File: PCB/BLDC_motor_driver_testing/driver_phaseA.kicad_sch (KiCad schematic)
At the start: 22 parts, among them Q1 IRF540N, Q2 IRF540N, U2 IR2104, U3 INA240A2D, U4 LMV393

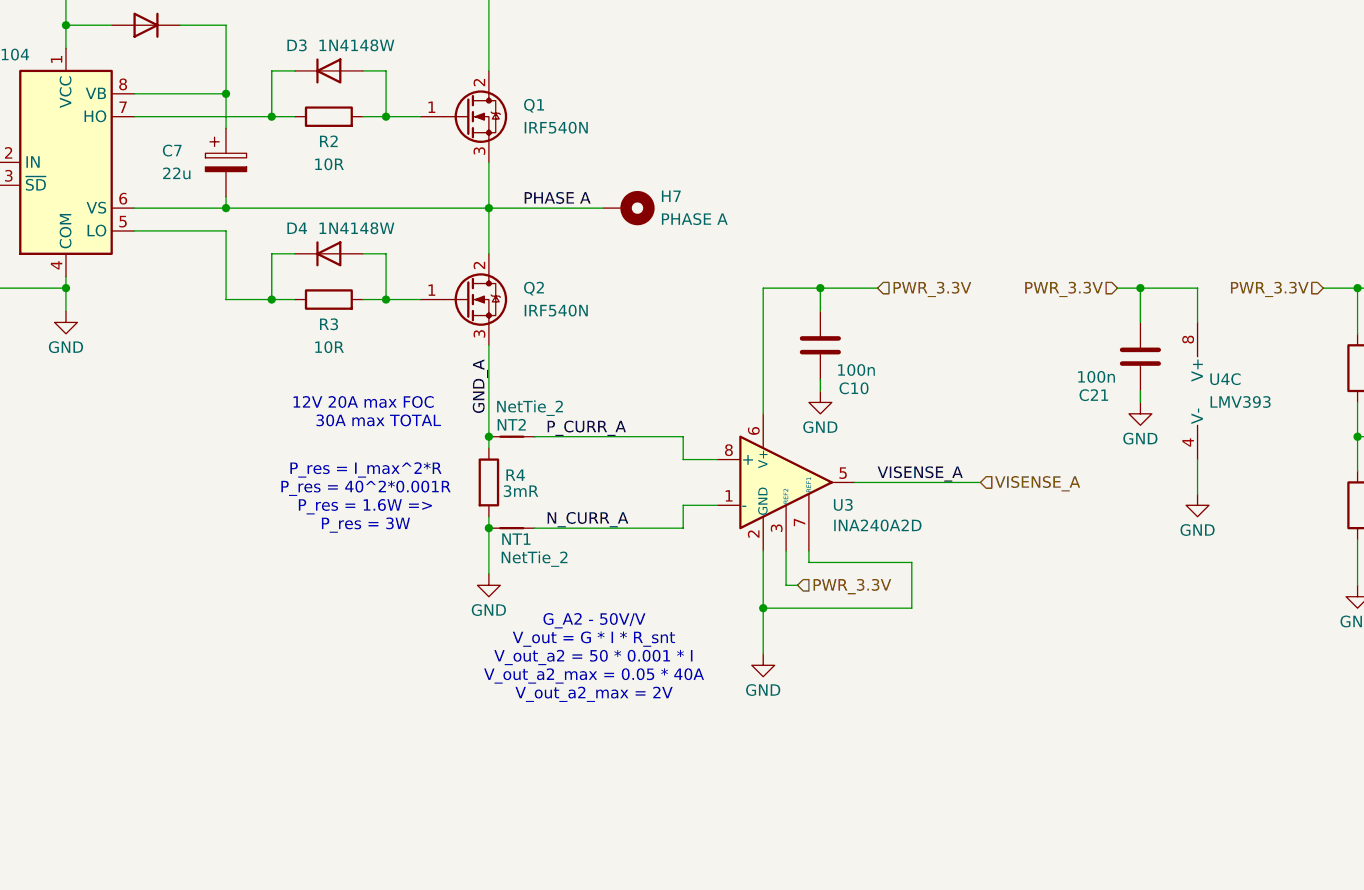
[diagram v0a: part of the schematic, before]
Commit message: selected bootstrap caps and shunt resistor and csa gain
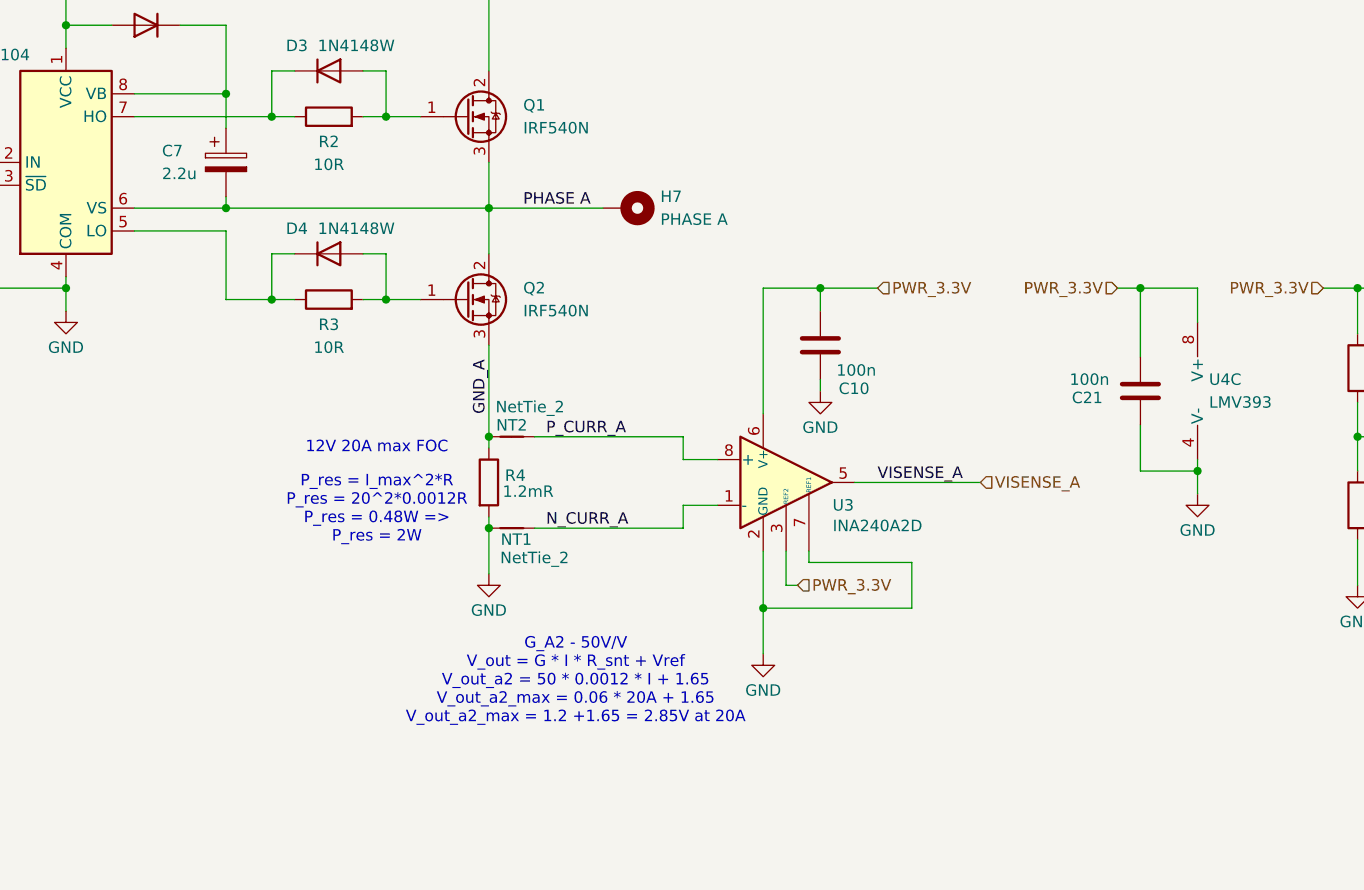
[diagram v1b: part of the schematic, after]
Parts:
- C7: value 22u -> 2.2u; footprint Capacitor_Tantalum_SMD:CP_EIA-3216-18_Kemet-A_HandSolder -> Capacitor_SMD:C_0805_2012Metric_Pad1.18x1.45mm_HandSolder
- R4: value 3mR -> 1.2mR
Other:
- note added: "12V 20A max FOC"
- note added: "G_A2 - 50V/V V_out = G * I * R_snt + Vref V_out_a2 = 50 * 0.0012 * I + 1.65 V_out_a2_max = 0.06 * 20A + 1.65 V_out_a2_max = 1.2 +1.65 = 2.85V at 20A"
- note added: "P_res = I_max^2*R P_res = 20^2*0.0012R P_res = 0.48W => P_res = 2W"
- note removed: "12V 20A max FOC 30A max TOTAL"
- note removed: "G_A2 - 50V/V V_out = G * I * R_snt V_out_a2 = 50 * 0.001 * I V_out_a2_max = 0.05 * 40A V_out_a2_max = 2V"
- note removed: "P_res = I_max^2*R P_res = 40^2*0.001R P_res = 1.6W => P_res = 3W"
- moved on the sheet: C21
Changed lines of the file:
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@@
 	(generator_version "9.0")
 	(paper "A4")
-	(text "12V 20A max FOC\n	  30A max TOTAL"
+	(text "12V 20A max FOC"
 		(exclude_from_sim no)
-		(at 99.06 107.95 0)
+		(at 100.584 111.76 0)
 		(effects
 			(font
@@
 		)
 	)
-	(text "G_A2 - 50V/V\nV_out = G * I * R_snt\nV_out_a2 = 50 * 0.001 * I\nV_out_a2_max = 0.05 * 40A\nV_out_a2_max = 2V"
+	(text "G_A2 - 50V/V\nV_out = G * I * R_snt + Vref\nV_out_a2 = 50 * 0.0012 * I + 1.65\nV_out_a2_max = 0.06 * 20A + 1.65\nV_out_a2_max = 1.2 +1.65 = 2.85V at 20A"
 		(exclude_from_sim no)
-		(at 124.714 135.128 0)
+		(at 122.682 137.668 0)
 		(effects
 			(font
@@
 		)
 	)
-	(text "P_res = I_max^2*R\nP_res = 40^2*0.001R\nP_res = 1.6W =>\nP_res = 3W"
+	(text "BLDC Driver Phase B"
 		(exclude_from_sim no)
-		(at 99.314 117.348 0)
+		(at 197.358 189.738 0)
 		(effects
 			(font
@@
 		)
 	)
-	(text "BLDC Driver Phase B"
+	(text "P_res = I_max^2*R\nP_res = 20^2*0.0012R\nP_res = 0.48W =>\nP_res = 2W"
 		(exclude_from_sim no)
-		(at 197.358 189.738 0)
+		(at 100.584 118.618 0)
 		(effects
 			(font
@@
 	)
 	(junction
+		(at 191.77 114.3)
+		(diameter 0)
+		(color 0 0 0 0)
+	)
+	(junction
 		(at 143.51 129.54)
 		(diameter 0)
@@
 	(wire
 		(pts
-			(xy 191.77 116.84) (xy 191.77 113.03)
+			(xy 191.77 116.84) (xy 191.77 114.3)
 		)
 		(stroke
@@
 	(wire
 		(pts
+			(xy 185.42 109.22) (xy 185.42 114.3)
+		)
+		(stroke
+			(width 0)
+			(type default)
+		)
+	)
+	(wire
+		(pts
 			(xy 143.51 129.54) (xy 160.02 129.54)
 		)
@@
 	(wire
 		(pts
-			(xy 185.42 105.41) (xy 185.42 106.68)
-		)
-		(stroke
-			(width 0)
-			(type default)
-		)
-	)
-	(wire
-		(pts
 			(xy 118.11 120.65) (xy 134.62 120.65)
 		)
@@
 	(wire
 		(pts
+			(xy 191.77 114.3) (xy 191.77 113.03)
+		)
+		(stroke
+			(width 0)
+			(type default)
+		)
+	)
+	(wire
+		(pts
 			(xy 91.44 69.85) (xy 88.9 69.85)
 		)
@@
 	(wire
 		(pts
-			(xy 185.42 97.79) (xy 185.42 93.98)
+			(xy 185.42 101.6) (xy 185.42 93.98)
 		)
 		(stroke
@@
 	(wire
 		(pts
+			(xy 185.42 114.3) (xy 191.77 114.3)
+		)
+		(stroke
+			(width 0)
+			(type default)
+		)
+	)
+	(wire
+		(pts
 			(xy 148.59 124.46) (xy 160.02 124.46)
 		)
@@
 			)
 		)
-		(property "Value" "3mR"
+		(property "Value" "1.2mR"
 			(at 114.554 116.586 0)
 			(effects
@@
 			)
 		)
-		(property "Value" "22u"
+		(property "Value" "2.2u"
 			(at 76.708 81.28 0)
 			(effects
@@
 			)
 		)
-		(property "Footprint" "Capacitor_Tantalum_SMD:CP_EIA-3216-18_Kemet-A_HandSolder"
+		(property "Footprint" "Capacitor_SMD:C_0805_2012Metric_Pad1.18x1.45mm_HandSolder"
 			(at 84.7852 83.82 0)
 			(effects
@@
 	(symbol
 		(lib_id "Device:C")
-		(at 185.42 101.6 0)
+		(at 185.42 105.41 0)
 		(unit 1)
 		(exclude_from_sim no)
@@
 		(dnp no)
 		(property "Reference" "C21"
-			(at 178.562 105.918 0)
+			(at 177.8 106.172 0)
 			(effects
 				(font
@@
 		)
 		(property "Value" "100n"
-			(at 178.308 103.886 0)
+			(at 177.546 104.14 0)
 			(effects
 				(font
@@
 		)
 		(property "Footprint" "Capacitor_SMD:C_0805_2012Metric_Pad1.18x1.45mm_HandSolder"
-			(at 186.3852 105.41 0)
+			(at 186.3852 109.22 0)
 			(effects
 				(font
@@
 		)
 		(property "Datasheet" "~"
-			(at 185.42 101.6 0)
+			(at 185.42 105.41 0)
 			(effects
 				(font
@@
 		)
 		(property "Description" "Unpolarized capacitor"
-			(at 185.42 101.6 0)
+			(at 185.42 105.41 0)
 			(effects
 				(font
@@
 					(unit 1)
 				)
-			)
-		)
-	)
-	(symbol
-		(lib_id "power:GND")
-		(at 185.42 106.68 0)
-		(unit 1)
-		(exclude_from_sim no)
-		(in_bom yes)
-		(on_board yes)
-		(dnp no)
-		(property "Reference" "#PWR039"
-			(at 185.42 113.03 0)
-			(effects
-				(font
-					(size 1.27 1.27)
-				)
-				(hide yes)
-			)
-		)
-		(property "Value" "GND"
-			(at 185.42 110.744 0)
-			(effects
-				(font
-					(size 1.27 1.27)
-				)
-			)
-		)
-		(property "Footprint" ""
-			(at 185.42 106.68 0)
-			(effects
-				(font
-					(size 1.27 1.27)
-				)
-				(hide yes)
-			)
-		)
-		(property "Datasheet" ""
-			(at 185.42 106.68 0)
-			(effects
-				(font
-					(size 1.27 1.27)
-				)
-				(hide yes)
-			)
-		)
-		(property "Description" "Power symbol creates a global label with name \"GND\" , ground"
-			(at 185.42 106.68 0)
-			(effects
-				(font
-					(size 1.27 1.27)
-				)
-				(hide yes)
-			)
-		)
-		(pin "1"
-		)
-		(instances
-			(project "BLDC_motor_driver_testing"
-				(path "/4ecc7e27-f6b5-41f4-b6cd-6ae03975803c/84a85dbb-6ec3-48bc-bc0c-ced3ee7759cd"
-					(reference "#PWR039")
-					(unit 1)
-				)

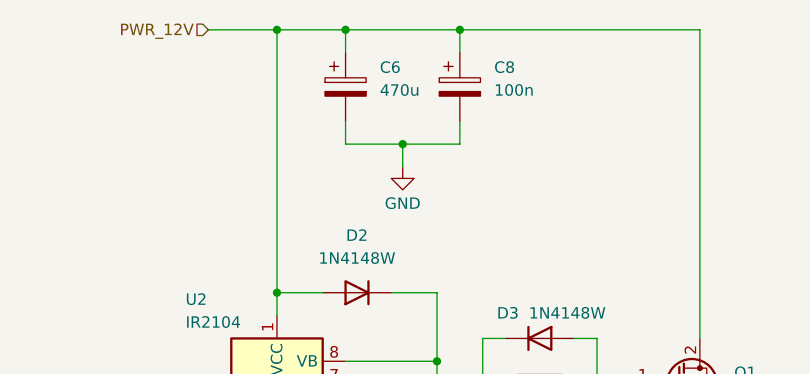
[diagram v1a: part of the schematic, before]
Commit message: Final version of BLDC test driver
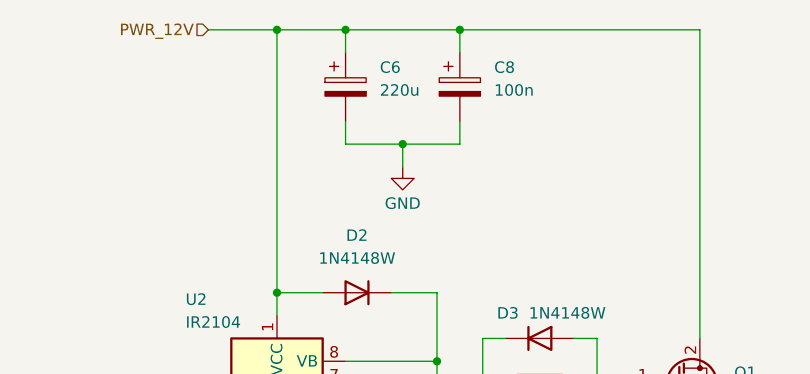
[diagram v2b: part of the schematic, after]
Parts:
- C6: value 470u -> 220u; JLCPCB Part # (none) -> C3340
- C7: JLCPCB Part # (none) -> C342739
- C8: JLCPCB Part # (none) -> C2976899
- R4: JLCPCB Part # (none) -> C51934143
- U3: JLCPCB Part # (none) -> C2060768
- U4: footprint Package_SO:VSSOP-8_2.3x2mm_P0.5mm -> Package_SO:VSSOP-8_3x3mm_P0.65mm; JLCPCB Part # (none) -> C352866
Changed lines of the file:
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@@
 			)
 		)
-		(property "Footprint" "Package_SO:VSSOP-8_2.3x2mm_P0.5mm"
+		(property "Footprint" "Package_SO:VSSOP-8_3x3mm_P0.65mm"
 			(at 240.03 107.95 0)
 			(effects
@@
 		)
 		(property "Description" "Dual General-Purpose Low-Voltage Comparator, SOIC-8/TSSOP-8/VSSOP-8"
+			(at 240.03 107.95 0)
+			(effects
+				(font
+					(size 1.27 1.27)
+				)
+				(hide yes)
+			)
+		)
+		(property "JLCPCB Part #" "C352866"
 			(at 240.03 107.95 0)
 			(effects
@@
 			)
 		)
+		(property "JLCPCB Part #" "C51934143"
+			(at 113.03 115.57 0)
+			(effects
+				(font
+					(size 1.27 1.27)
+				)
+				(hide yes)
+			)
+		)
 		(pin "1"
 		)
@@
 			)
 		)
-		(property "Value" "470u"
+		(property "Value" "220u"
 			(at 77.47 42.2909 0)
 			(effects
@@
 			)
 		)
+		(property "JLCPCB Part #" "C3340"
+			(at 73.66 41.91 0)
+			(effects
+				(font
+					(size 1.27 1.27)
+				)
+				(hide yes)
+			)
+		)
 		(pin "1"
 		)
@@
 		)
 		(property "Description" "High- and Low-Side, Bidirectional, Zero-Drift, Current-Sense Amplifier With Enhanced PWM Rejection, 50V/V, SOIC-8"
+			(at 146.05 115.57 0)
+			(effects
+				(font
+					(size 1.27 1.27)
+				)
+				(hide yes)
+			)
+		)
+		(property "JLCPCB Part #" "C2060768"
 			(at 146.05 115.57 0)
 			(effects
@@
 			)
 		)
+		(property "JLCPCB Part #" "C2976899"
+			(at 86.36 41.91 0)
+			(effects
+				(font
+					(size 1.27 1.27)
+				)
+				(hide yes)
+			)
+		)
 		(pin "2"
 		)
@@
 		)
 		(property "Description" "Polarized capacitor"
+			(at 83.82 80.01 0)
+			(effects
+				(font
+					(size 1.27 1.27)
+				)
+				(hide yes)
+			)
+		)
+		(property "JLCPCB Part #" "C342739"
 			(at 83.82 80.01 0)
 			(effects
@@
 			)
 		)
-		(property "Footprint" "Package_SO:VSSOP-8_2.3x2mm_P0.5mm"
+		(property "Footprint" "Package_SO:VSSOP-8_3x3mm_P0.65mm"
 			(at 240.03 124.46 0)
 			(effects
@@
 		)
 		(property "Description" "Dual General-Purpose Low-Voltage Comparator, SOIC-8/TSSOP-8/VSSOP-8"
+			(at 240.03 124.46 0)
+			(effects
+				(font
+					(size 1.27 1.27)
+				)
+				(hide yes)
+			)
+		)
+		(property "JLCPCB Part #" "C352866"
 			(at 240.03 124.46 0)
 			(effects
@@
 			)
 		)
-		(property "Footprint" "Package_SO:VSSOP-8_2.3x2mm_P0.5mm"
+		(property "Footprint" "Package_SO:VSSOP-8_3x3mm_P0.65mm"
 			(at 194.31 105.41 0)
 			(effects
@@
 			(at 194.31 105.41 0)
 			(effects
+				(font
+					(size 1.27 1.27)
+				)
+				(hide yes)
+			)
+		)
+		(property "JLCPCB Part #" "C352866"
+			(at 194.31 105.41 0)
+			(effects
